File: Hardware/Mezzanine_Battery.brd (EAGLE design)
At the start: 30.5 x 44.5 mm, 24 parts, among them U1 MCP73831, U2 EDISON_CONNECTOR_FULLMOUNTING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, U3 EDISON_CONNECTOR_FULLHEADER

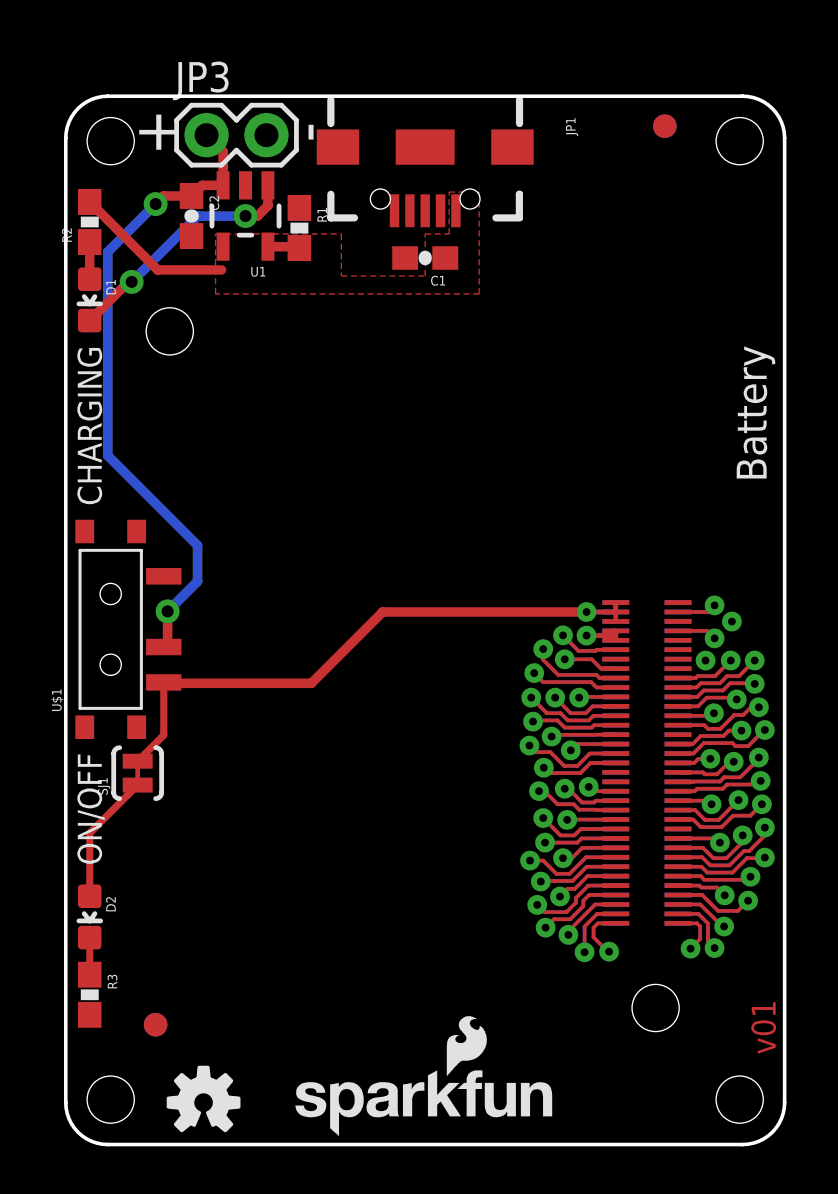
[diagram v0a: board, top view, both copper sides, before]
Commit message: corrected names, added DCIN, cleaned up dimensions
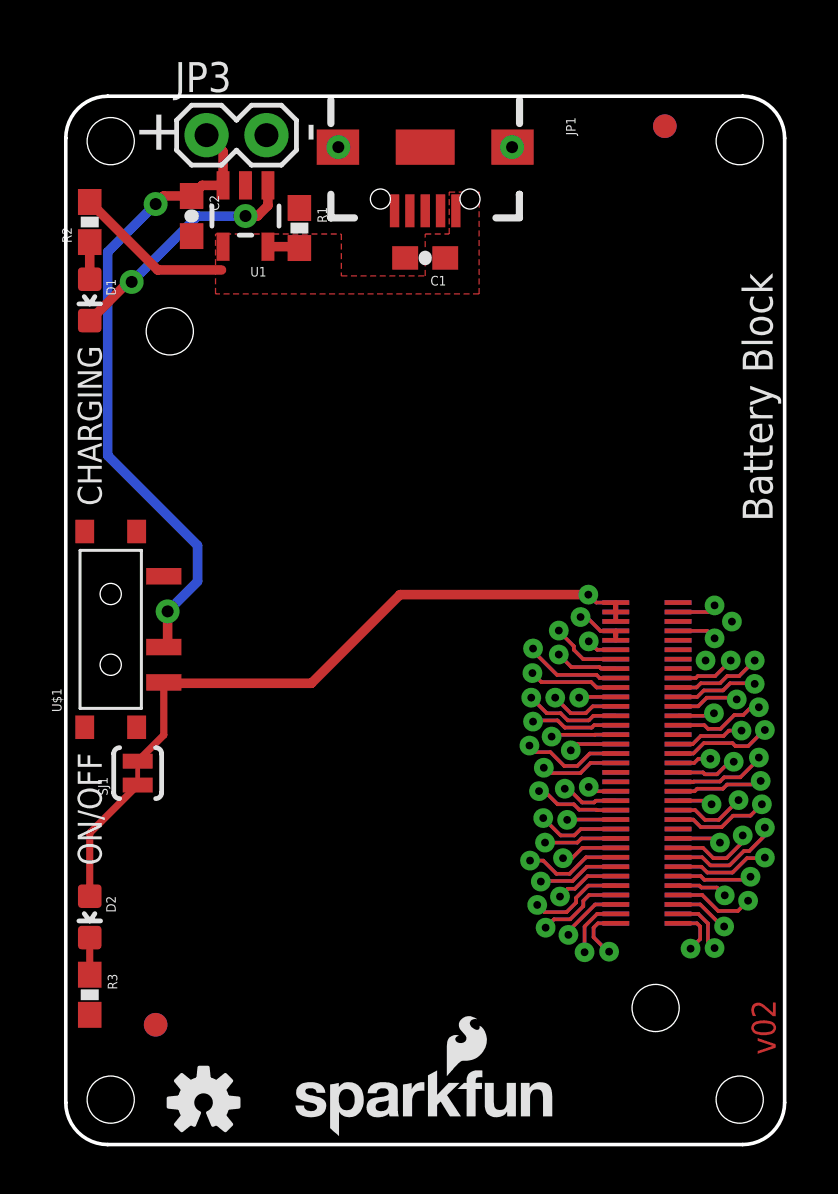
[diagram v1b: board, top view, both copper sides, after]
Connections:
- new net DCIN: U2.14, U3.14
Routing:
- net DCIN: track 0.00 -> 6.05 mm, vias 0 -> 1
- net 1.8V: track 5.07 -> 2.95 mm
- net 3.3V: track 3.68 -> 4.47 mm
- net USB_DP: track 4.65 -> 5.33 mm
- net VSYS: track 27.5 -> 28.0 mm
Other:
- board text added: "Battery Block"
- board text added: "Note: Units are in Inches"
- board text added: "v02"
- board text removed: "Battery"
- board text removed: "Connectors Go Here"
- board text removed: "LED's and selector switches go here"
- board text removed: "Max Board Length"
- board text removed: "Nothing goes here... I mean it."
- board text removed: "v01"
